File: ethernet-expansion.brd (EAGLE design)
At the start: 64.4 x 38.1 mm, 21 parts, among them Q1 25MHz, U1 ENC28J60-SO

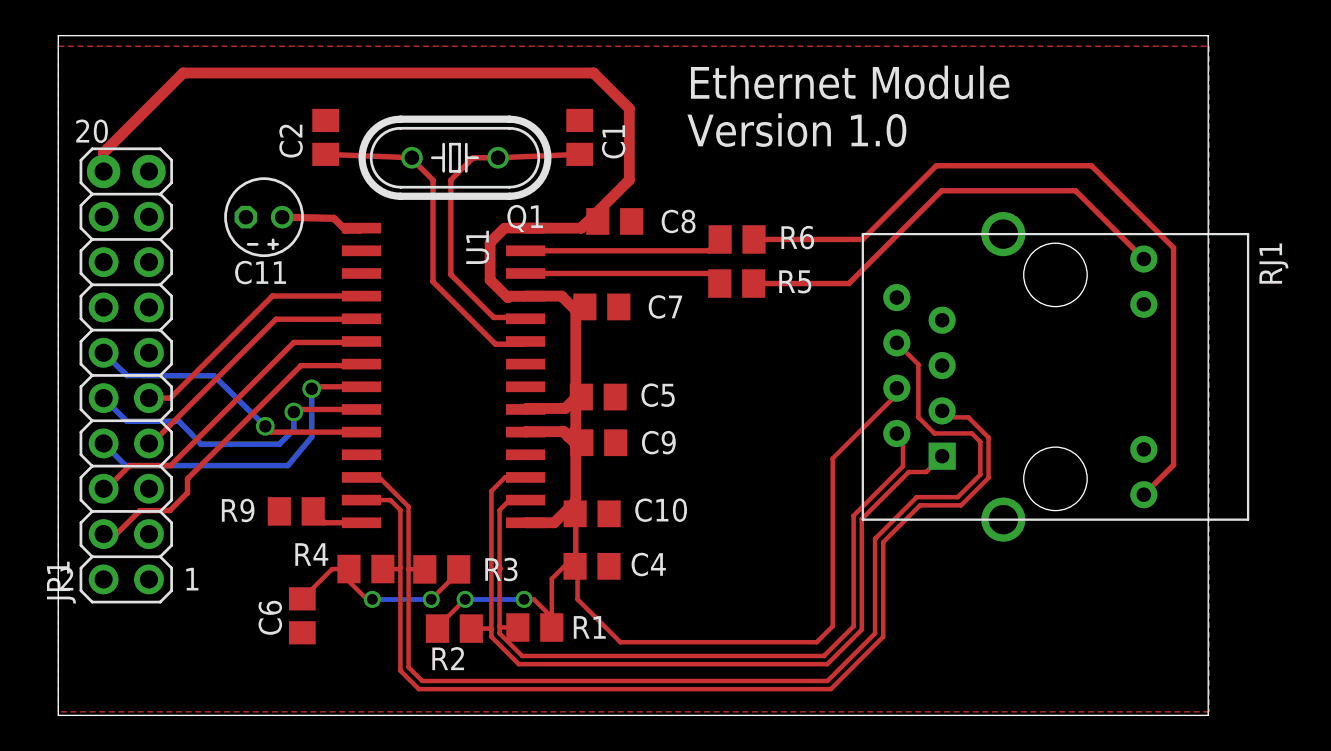
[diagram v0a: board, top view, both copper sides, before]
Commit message: Recreated the ground fill to fix the last error
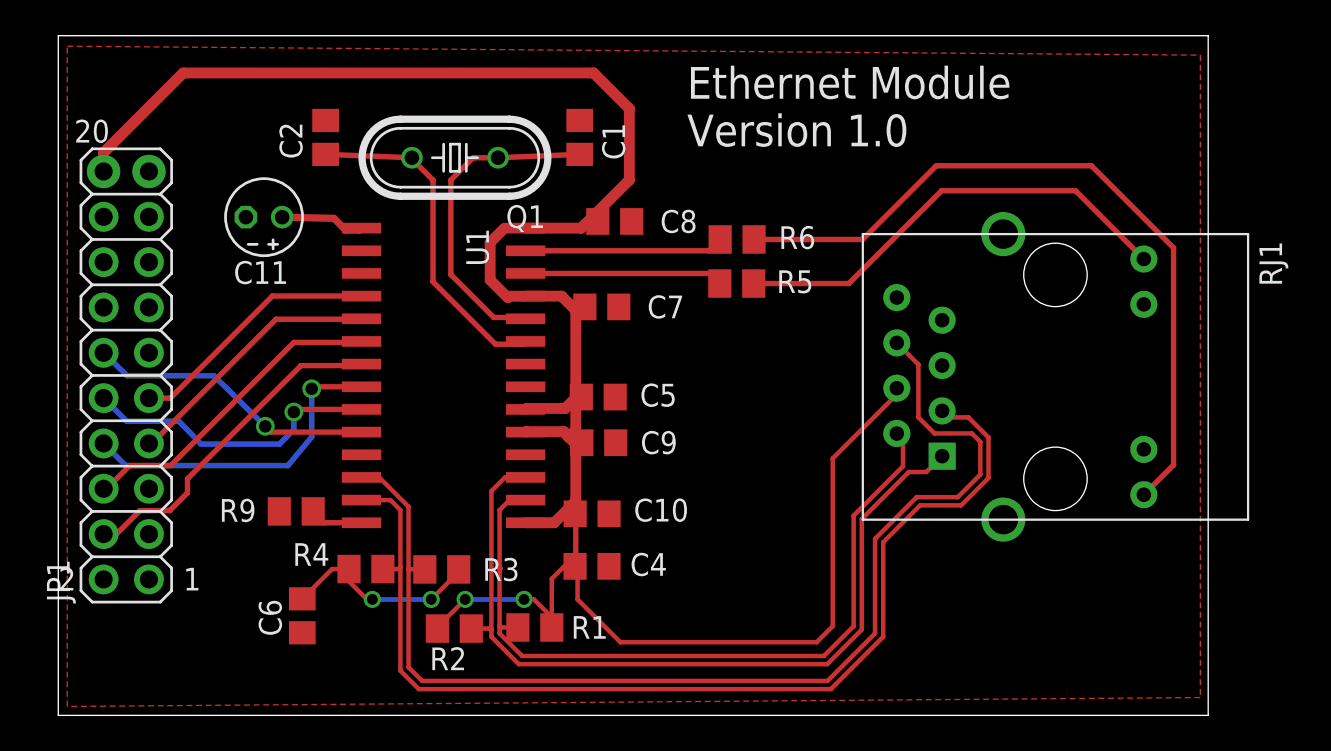
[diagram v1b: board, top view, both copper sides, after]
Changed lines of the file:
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@@
 <layer number="27" name="tValues" color="7" fill="1" visible="yes" active="yes"/>
 <layer number="28" name="bValues" color="7" fill="1" visible="yes" active="yes"/>
-<layer number="29" name="tStop" color="7" fill="3" visible="yes" active="yes"/>
-<layer number="30" name="bStop" color="7" fill="6" visible="yes" active="yes"/>
+<layer number="29" name="tStop" color="7" fill="3" visible="no" active="yes"/>
+<layer number="30" name="bStop" color="7" fill="6" visible="no" active="yes"/>
 <layer number="31" name="tCream" color="7" fill="4" visible="yes" active="yes"/>
 <layer number="32" name="bCream" color="7" fill="5" visible="yes" active="yes"/>
@@
 <contactref element="JP1" pad="1"/>
 <contactref element="C11" pad="-"/>
-<polygon width="0.1" layer="1" isolate="0.5">
-<vertex x="0" y="37.5"/>
-<vertex x="64.5" y="37.5"/>
-<vertex x="64.5" y="0.2"/>
-<vertex x="0" y="0.2"/>
+<polygon width="0.254" layer="1" isolate="0.5">
+<vertex x="0.5" y="37.5"/>
+<vertex x="64" y="37"/>
+<vertex x="64" y="1"/>
+<vertex x="0.5" y="0.5"/>
 </polygon>
-<wire x1="31.21" y1="17.84" x2="26.19" y2="18.415" width="0" layer="19" extent="1-1"/>
 </signal>
 <signal name="N$8">

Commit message: Adding dru and cam file from Seeed studio and moving traces to make the ground fill more complete
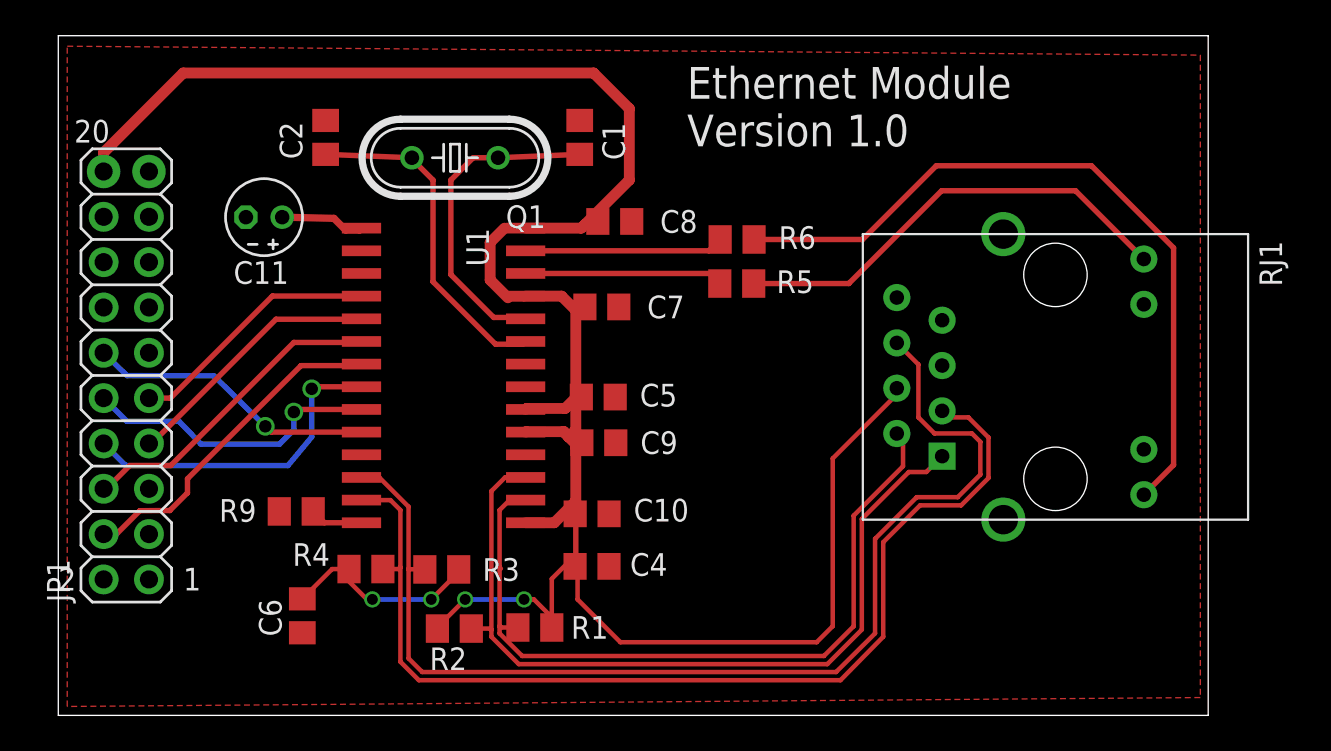
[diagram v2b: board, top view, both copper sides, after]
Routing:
- net TPIN_N: track 64.0 -> 63.3 mm
- net TPIN_P: track 59.3 -> 58.6 mm
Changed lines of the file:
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@@
 </class>
 </classes>
-<designrules name="LaenPCBOrder">
+<designrules name="SeeedStudio_2layer_DRU_no_angle_20140221">
 <description language="de">&lt;b&gt;EAGLE Design Rules&lt;/b&gt;
 &lt;p&gt;
@@
 Einstellungen hier und speichern die Design Rules unter
 einem neuen Namen ab.</description>
-<description language="en">&lt;b&gt;Laen's PCB Order Design Rules&lt;/b&gt;
+<description language="en">&lt;b&gt;EAGLE Design Rules&lt;/b&gt;
 &lt;p&gt;
-Please make sure your boards conform to these design rules.</description>
+The default Design Rules have been set to cover
+a wide range of applications. Your particular design
+may have different requirements, so please make the
+necessary adjustments and save your customized
+design rules under a new name.</description>
+<description language="zh">&lt;b&gt;Seeed Studio EAGLE Design Rules&lt;/b&gt;
+</description>
 <param name="layerSetup" value="(1*16)"/>
-<param name="mtCopper" value="0.0356mm 0.0356mm 0.0356mm 0.0356mm 0.0356mm 0.0356mm 0.0356mm 0.0356mm 0.0356mm 0.0356mm 0.0356mm 0.0356mm 0.0356mm 0.0356mm 0.0356mm 0.0356mm"/>
-<param name="mtIsolate" value="1.5011mm 0.1499mm 0.2007mm 0.1499mm 0.2007mm 0.1499mm 0.2007mm 0.1499mm 0.2007mm 0.1499mm 0.2007mm 0.1499mm 0.2007mm 0.1499mm 0.2007mm"/>
+<param name="mtCopper" value="0.035mm 0.0175mm 0.035mm 0.035mm 0.035mm 0.035mm 0.035mm 0.035mm 0.035mm 0.035mm 0.035mm 0.035mm 0.035mm 0.035mm 0.0175mm 0.035mm"/>
+<param name="mtIsolate" value="1.5mm 1.1mm 0.2mm 0.15mm 0.2mm 0.15mm 0.2mm 0.15mm 0.2mm 0.15mm 0.2mm 0.15mm 0.2mm 0.15mm 0.2mm"/>
 <param name="mdWireWire" value="6mil"/>
 <param name="mdWirePad" value="6mil"/>
@@
 <param name="mdPadVia" value="6mil"/>
 <param name="mdViaVia" value="6mil"/>
-<param name="mdSmdPad" value="6mil"/>
-<param name="mdSmdVia" value="6mil"/>
-<param name="mdSmdSmd" value="6mil"/>
+<param name="mdSmdPad" value="0mil"/>
+<param name="mdSmdVia" value="0mil"/>
+<param name="mdSmdSmd" value="0mil"/>
 <param name="mdViaViaSameLayer" value="8mil"/>
 <param name="mnLayersViaInSmd" value="2"/>
-<param name="mdCopperDimension" value="15mil"/>
-<param name="mdDrill" value="6mil"/>
+<param name="mdCopperDimension" value="10mil"/>
+<param name="mdDrill" value="10mil"/>
 <param name="mdSmdStop" value="0mil"/>
 <param name="msWidth" value="6mil"/>
-<param name="msDrill" value="13mil"/>
-<param name="msMicroVia" value="13mil"/>
+<param name="msDrill" value="12mil"/>
+<param name="msMicroVia" value="12mil"/>
 <param name="msBlindViaRatio" value="0.5"/>
 <param name="rvPadTop" value="0.25"/>
@@
 <param name="rvMicroViaOuter" value="0.25"/>
 <param name="rvMicroViaInner" value="0.25"/>
-<param name="rlMinPadTop" value="7mil"/>
+<param name="rlMinPadTop" value="10mil"/>
 <param name="rlMaxPadTop" value="20mil"/>
-<param name="rlMinPadInner" value="7mil"/>
+<param name="rlMinPadInner" value="10mil"/>
 <param name="rlMaxPadInner" value="20mil"/>
-<param name="rlMinPadBottom" value="7mil"/>
+<param name="rlMinPadBottom" value="10mil"/>
 <param name="rlMaxPadBottom" value="20mil"/>
-<param name="rlMinViaOuter" value="7mil"/>
+<param name="rlMinViaOuter" value="6mil"/>
 <param name="rlMaxViaOuter" value="20mil"/>
-<param name="rlMinViaInner" value="7mil"/>
+<param name="rlMinViaInner" value="6mil"/>
 <param name="rlMaxViaInner" value="20mil"/>
 <param name="rlMinMicroViaOuter" value="4mil"/>
@@
 <param name="psTop" value="-1"/>
 <param name="psBottom" value="-1"/>
-<param name="psFirst" value="-1"/>
+<param name="psFirst" value="0"/>
 <param name="psElongationLong" value="100"/>
 <param name="psElongationOffset" value="100"/>
 <param name="mvStopFrame" value="1"/>
 <param name="mvCreamFrame" value="0"/>
-<param name="mlMinStopFrame" value="3mil"/>
-<param name="mlMaxStopFrame" value="3mil"/>
+<param name="mlMinStopFrame" value="2mil"/>
+<param name="mlMaxStopFrame" value="2mil"/>
 <param name="mlMinCreamFrame" value="0mil"/>
 <param name="mlMaxCreamFrame" value="0mil"/>
-<param name="mlViaStopLimit" value="0mil"/>
+<param name="mlViaStopLimit" value="100mil"/>
 <param name="srRoundness" value="0"/>
 <param name="srMinRoundness" value="0mil"/>
@@
 <param name="checkAngle" value="0"/>
 <param name="checkFont" value="1"/>
-<param name="checkRestrict" value="1"/>
+<param name="checkRestrict" value="0"/>
 <param name="useDiameter" value="13"/>
 <param name="maxErrors" value="50"/>
@@
 <wire x1="18.61170625" y1="12.065" x2="19.1714" y2="11.50530625" width="0.254" layer="1"/>
 <wire x1="19.1714" y1="11.50530625" x2="19.1714" y2="8.3" width="0.254" layer="1"/>
-<wire x1="19.1714" y1="8.3" x2="19.1714" y2="2.50530625" width="0.254" layer="1"/>
-<wire x1="19.1714" y1="2.50530625" x2="20.20530625" y2="1.4714" width="0.254" layer="1"/>
-<wire x1="20.20530625" y1="1.4714" x2="43.29469375" y2="1.4714" width="0.254" layer="1"/>
-<wire x1="43.29469375" y1="1.4714" x2="46.2286" y2="4.40530625" width="0.254" layer="1"/>
+<wire x1="19.1714" y1="8.3" x2="19.1714" y2="3.00530625" width="0.254" layer="1"/>
+<wire x1="19.1714" y1="3.00530625" x2="20.20530625" y2="1.9714" width="0.254" layer="1"/>
+<wire x1="20.20530625" y1="1.9714" x2="43.83469375" y2="1.9714" width="0.254" layer="1"/>
+<wire x1="43.83469375" y1="1.9714" x2="46.2286" y2="4.40530625" width="0.254" layer="1"/>
 <wire x1="46.2286" y1="4.40530625" x2="46.2286" y2="9.70530625" width="0.254" layer="1"/>
 <wire x1="46.2286" y1="9.70530625" x2="48.29469375" y2="11.7714" width="0.254" layer="1"/>
@@
 <wire x1="17.98829375" y1="13.335" x2="19.6286" y2="11.69469375" width="0.254" layer="1"/>
 <wire x1="19.6286" y1="11.69469375" x2="19.6286" y2="8.2" width="0.254" layer="1"/>
-<wire x1="19.6286" y1="8.2" x2="19.6286" y2="2.69469375" width="0.254" layer="1"/>
-<wire x1="19.6286" y1="2.69469375" x2="20.39469375" y2="1.9286" width="0.254" layer="1"/>
-<wire x1="20.39469375" y1="1.9286" x2="43.10530625" y2="1.9286" width="0.254" layer="1"/>
-<wire x1="43.10530625" y1="1.9286" x2="45.7714" y2="4.59469375" width="0.254" layer="1"/>
+<wire x1="19.6286" y1="8.2" x2="19.6286" y2="3.19469375" width="0.254" layer="1"/>
+<wire x1="19.6286" y1="3.19469375" x2="20.39469375" y2="2.4286" width="0.254" layer="1"/>
+<wire x1="20.39469375" y1="2.4286" x2="43.58530625" y2="2.4286" width="0.254" layer="1"/>
+<wire x1="43.58530625" y1="2.4286" x2="45.7714" y2="4.59469375" width="0.254" layer="1"/>
 <wire x1="45.7714" y1="4.59469375" x2="45.7714" y2="9.89469375" width="0.254" layer="1"/>
 <wire x1="45.7714" y1="9.89469375" x2="48.10530625" y2="12.2286" width="0.254" layer="1"/>
